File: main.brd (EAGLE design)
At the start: 50.8 x 50.8 mm, 83 parts, among them Q1 5.8A/30V/35mΩ, Q2 5.8A/30V/35mΩ, Q3 2.5A/30V/105mΩ, U2 SN65HVD32_D_8

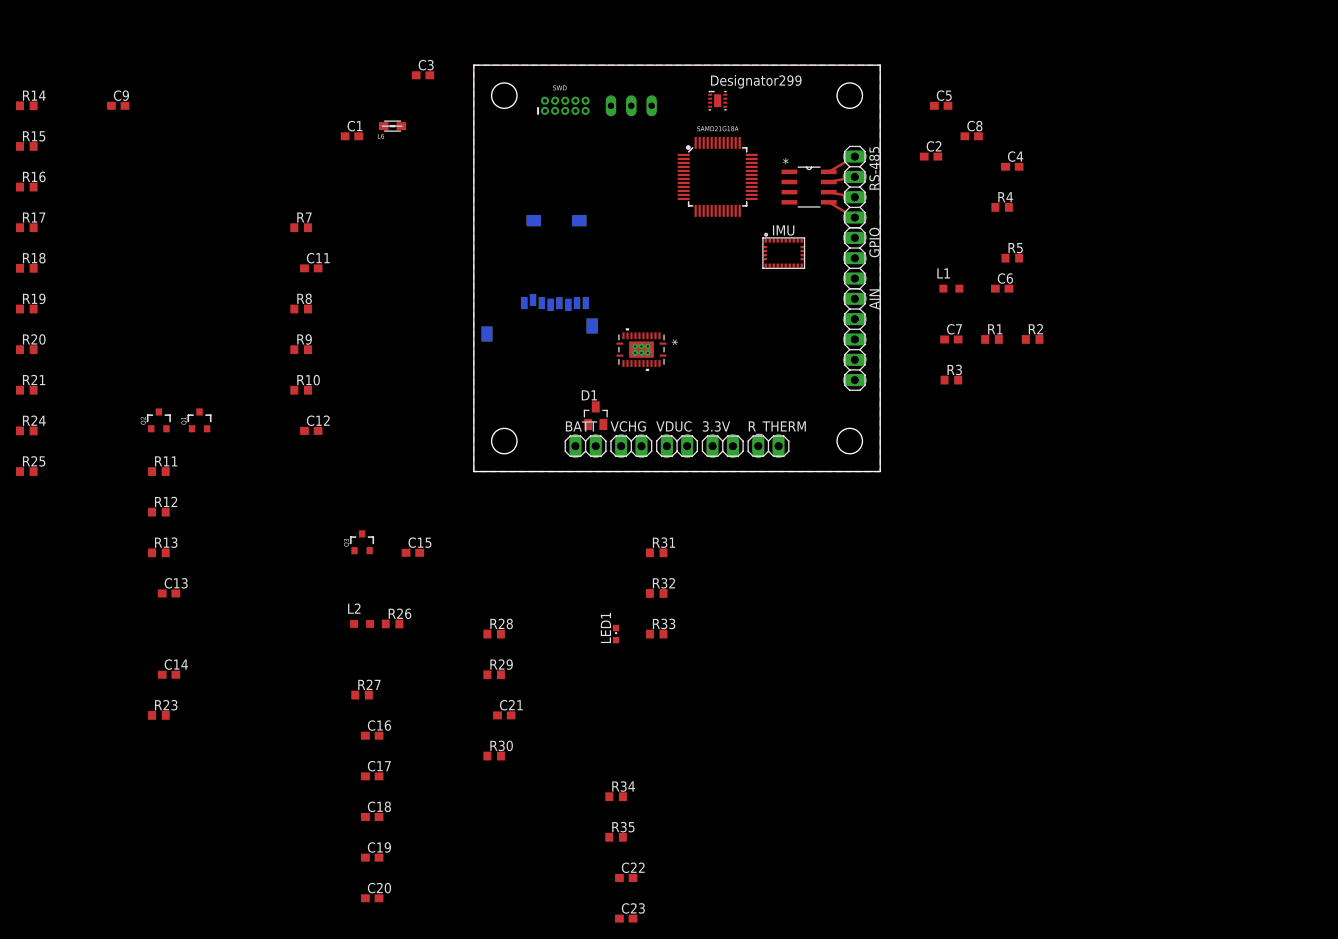
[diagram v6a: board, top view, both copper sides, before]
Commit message: Assembled alot of the board layout
Mostly charge controller elements
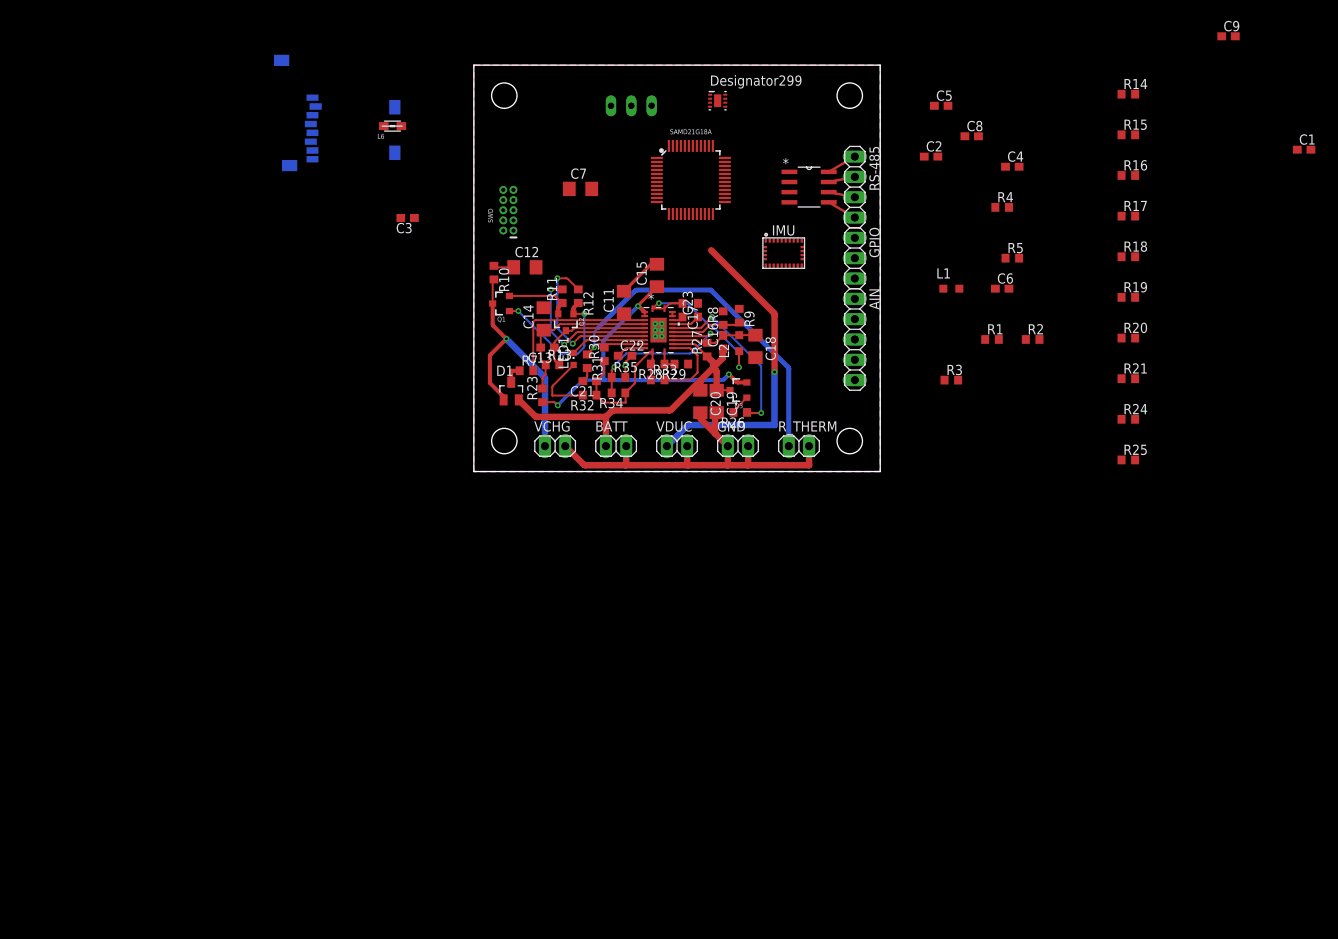
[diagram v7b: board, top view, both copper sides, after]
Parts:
- removed 3.3V: (no value), pinhead:1X02
- added GND: (no value), pinhead:1X02
- C11, C12, C14, C15, C18, C19, C20, C7: device resistor:C0603 -> rcl:C1206
- moved C9 139.1 mm to (94.3, 54.4)
- moved R14 137.7 mm to (81.8, 47.2)
- moved R15 137.7 mm to (81.8, 42.1)
- moved R16 137.7 mm to (81.8, 37.0)
- moved R17 137.7 mm to (81.8, 31.9)
- moved R18 137.7 mm to (81.8, 26.8)
- moved R19 137.7 mm to (81.8, 21.8)
- moved R20 137.7 mm to (81.8, 16.7)
- moved R21 137.7 mm to (81.8, 11.6)
- moved R24 137.7 mm to (81.8, 6.53)
- moved R25 137.7 mm to (81.8, 1.45)
- moved C1 119.0 mm to (103.8, 40.2)
- moved C23 76.6 mm to (28.0, 20.2), turned to 90 degrees
- moved C18 75.9 mm to (35.2, 15.6), turned to 270 degrees
- moved C20 74.4 mm to (28.3, 8.76), turned to 270 degrees
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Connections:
- removed net PC_CAN: POWER_CONTROLLER.5
- removed net V_BATT: D1.1
- net 3.3V: no longer 3.3V.1
- net GND: now also GND.1, GND.2; no longer 3.3V.2
- net PC_ACN: now also POWER_CONTROLLER.5
- net PC_SRN: now also D1.2
- net VIN: now also D1.1; no longer D1.2
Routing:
- net GND: track 0.00 -> 63.1 mm, vias 0 -> 1
- net PC_TS: track 0.00 -> 49.9 mm, vias 0 -> 1
- net PC_SRN: track 0.00 -> 46.8 mm
- net PC_PVCC: track 0.00 -> 44.2 mm, vias 0 -> 3
- net VSYS: track 0.00 -> 39.6 mm, vias 0 -> 1
- net VIN: track 0.00 -> 32.7 mm, vias 0 -> 1
- net PC_ACSET: track 0.00 -> 22.1 mm, vias 0 -> 2
- net PC_NBATDRV: track 0.00 -> 21.8 mm, vias 0 -> 2
- net PC_ACDRV: track 0.00 -> 21.5 mm, vias 0 -> 2
- net PC_SW: track 0.00 -> 21.4 mm, vias 0 -> 2
- net PC_AVCC: track 0.00 -> 20.9 mm
- net PC_ACN: track 0.00 -> 20.7 mm
- net PC_VREF: track 0.00 -> 20.2 mm
- net PC_CMSRC: track 0.00 -> 19.7 mm, vias 0 -> 2
- net N$17: track 0.00 -> 19.0 mm, vias 0 -> 2
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
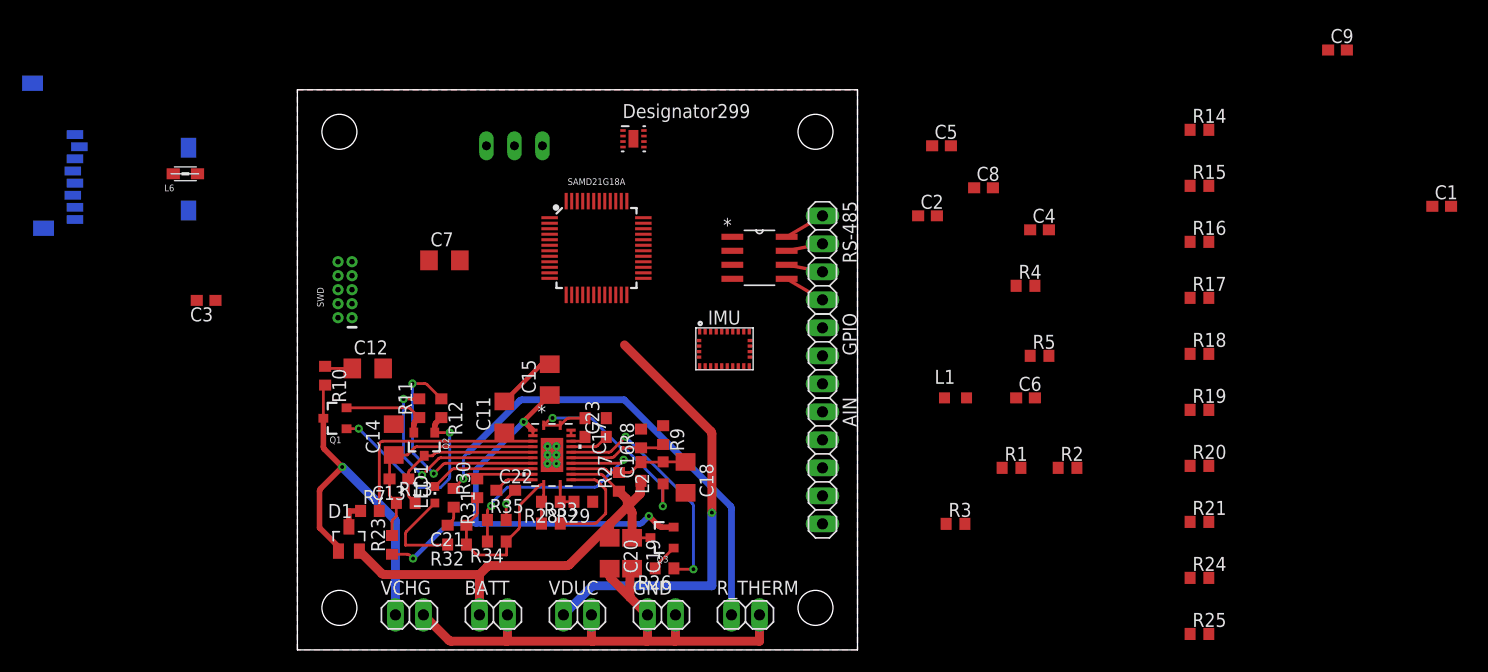
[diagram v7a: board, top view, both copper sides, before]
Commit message: Finished board Layout
First attempt at a board layout for the schematic, most likley not final.
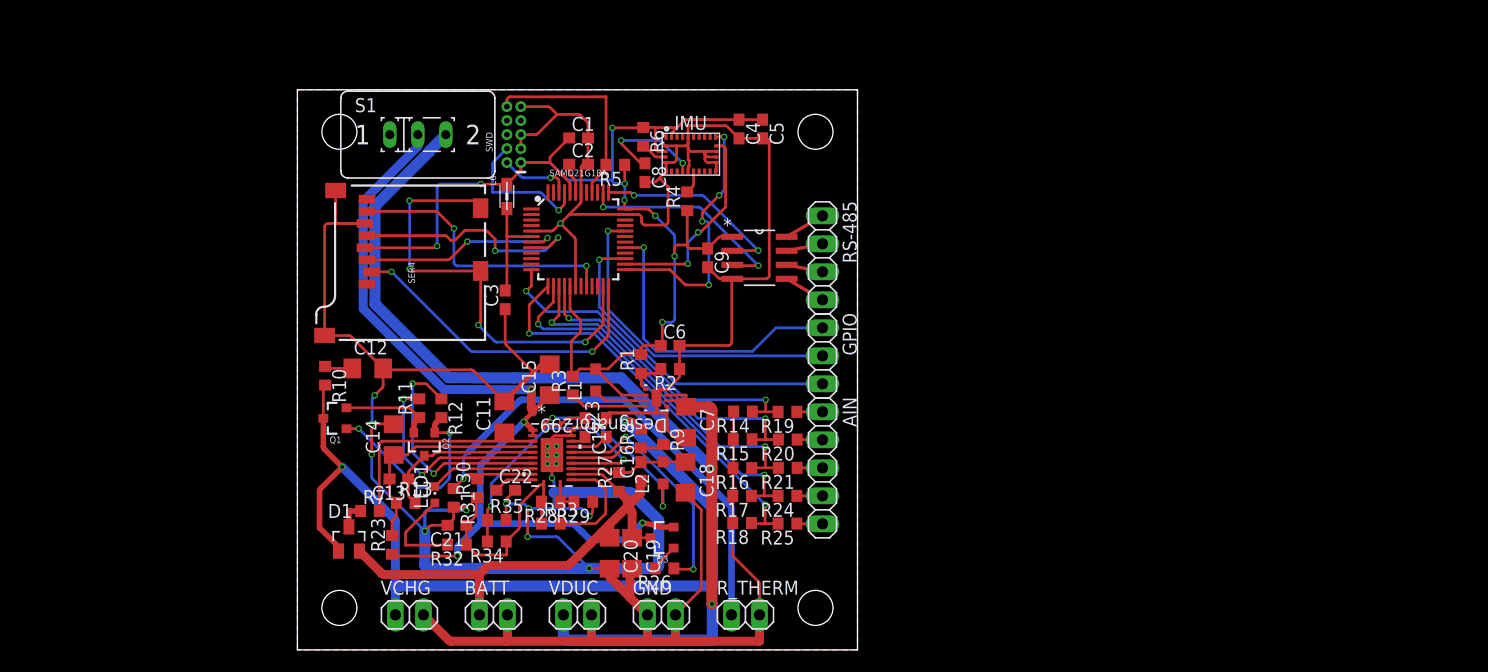
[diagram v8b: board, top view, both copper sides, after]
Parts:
- added R6: 10k, resistor:R0603
- moved C1 78.5 mm to (25.5, 46.4)
- moved C9 60.2 mm to (37.2, 35.6), turned to 270 degrees
- moved R14 48.7 mm to (40.4, 21.6), turned to 180 degrees
- moved R15 47.4 mm to (40.4, 19.1), turned to 180 degrees
- moved R16 46.3 mm to (40.4, 16.5), turned to 180 degrees
- moved R17 45.2 mm to (40.3, 14.0), turned to 180 degrees
- moved R18 44.2 mm to (40.3, 11.5), turned to 180 degrees
- moved R5 42.2 mm to (28.8, 44.0), turned to 180 degrees
- moved R25 38.7 mm to (44.5, 11.5), turned to 180 degrees
- moved R24 38.1 mm to (44.5, 14.0), turned to 180 degrees
- moved R21 37.7 mm to (44.5, 16.5), turned to 180 degrees
- moved R20 37.4 mm to (44.5, 19.1), turned to 180 degrees
- moved R19 37.4 mm to (44.5, 21.6), turned to 180 degrees
- moved R2 37.1 mm to (33.8, 25.5), turned to 180 degrees
- moved R3 36.9 mm to (25.0, 24.0), turned to 90 degrees
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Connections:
- net *INT renamed IMU_INT
- removed net *I2C_ADDR_SEL: IMU.17
- removed net *I2C_SCL: IMU.19
- removed net *I2C_SDA: IMU.20
- removed net *NBL_IMU: IMU.4
- removed net *XIN32: IMU.27
- removed net *XOUT32: IMU.26
- new net N$18: IMU.4, R6.2
- new net PA16_SER1_I2C_SDA: IMU.20, SAMD21G18A.25
- new net PA17_SER1_I2C_SCL: IMU.19, SAMD21G18A.26
- new net SWD_NRES: R5.2, SAMD21G18A.40, SWD.10
- net 3.3V: now also R6.1, SAMD21G18A.17, SAMD21G18A.36
- net AIN0: now also SAMD21G18A.12
- net AIN1: now also SAMD21G18A.16
- net AIN2: now also SAMD21G18A.15
- net AIN3: now also SAMD21G18A.14
- net AIN4: now also SAMD21G18A.13
- net GND: now also IMU.17
- net GPIO1: now also SAMD21G18A.29
- net GPIO2: now also SAMD21G18A.32
- net GPIO3: now also SAMD21G18A.27
- net NRESET: no longer R5.2, SAMD21G18A.40, SWD.10
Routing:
- net GND: track 63.1 -> 359.1 mm, vias 1 -> 12
- net 3.3V: track 0.00 -> 116.9 mm, vias 0 -> 8
- net VSYS: track 39.6 -> 98.2 mm, vias 1 -> 2
- net VIN: track 32.7 -> 81.6 mm, vias 1 -> 2
- net PA14_PORT: track 0.00 -> 40.7 mm, vias 0 -> 4
- net PC_PVCC: track 44.2 -> 82.6 mm, vias 3 -> 4
- net AIN4: track 0.00 -> 37.0 mm, vias 0 -> 2
- net AIN3: track 0.00 -> 34.5 mm, vias 0 -> 2
- net AIN2: track 0.00 -> 32.0 mm, vias 0 -> 2
- net AIN0: track 0.00 -> 31.4 mm, vias 0 -> 2
- net GPIO2: track 0.00 -> 29.9 mm, vias 0 -> 1
- net GPIO3: track 0.00 -> 29.8 mm, vias 0 -> 1
- net PA15_PORT: track 0.00 -> 29.5 mm, vias 0 -> 2
- net AIN1: track 0.00 -> 29.0 mm, vias 0 -> 2
- net GPIO1: track 0.00 -> 27.6 mm, vias 0 -> 1
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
